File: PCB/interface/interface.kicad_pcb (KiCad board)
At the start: 2 copper layers, 100 x 100 mm, 120 parts, among them J1 24VAC, J10 RS485, J2 Brake, J3 Motor, J4 Limit, J5 LED_G, J6 Ground, J7 LED_B, J8 UART, J9 POT, K1 G2R-1-E, K2 G2R-1-E, K3 G2R-1-E, K4 G2R-1-E, SW1 SW_SPST, U1 DCDC-isolator, U10 PC817, U11 74HCT595, U12 ESP-07, U13 AT24C64, U14 LM358, U15 HCNR201, U16 PC817, U17 LM358, U18 6N137, U19 MAX485E, U2 L7812, U20 6N137, U3 DCDC-isolator, U4 ULN2003A, U5 AMS1117-3.3, U6 PC817, U7 PC817, U8 PC817, U9 PC817

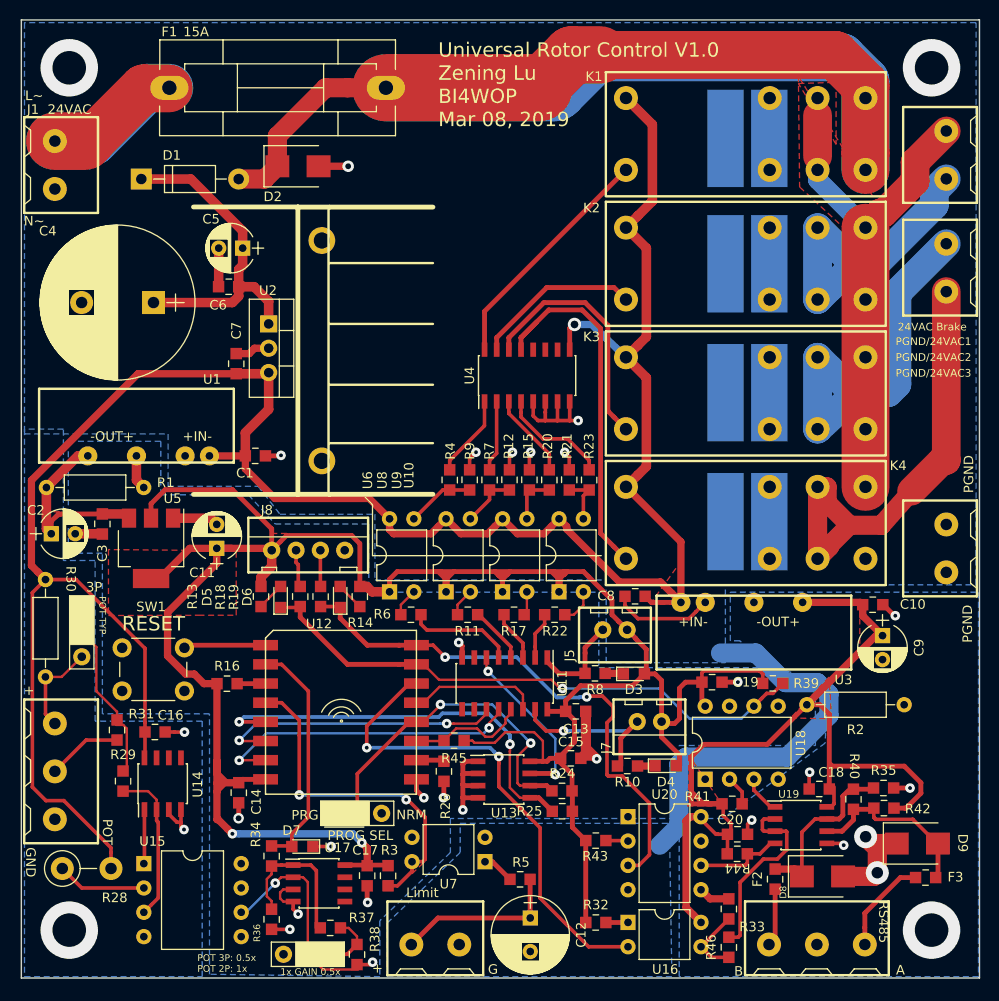
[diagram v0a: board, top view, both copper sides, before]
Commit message: New schemetic and PCB with support of Ethernet LAN connection
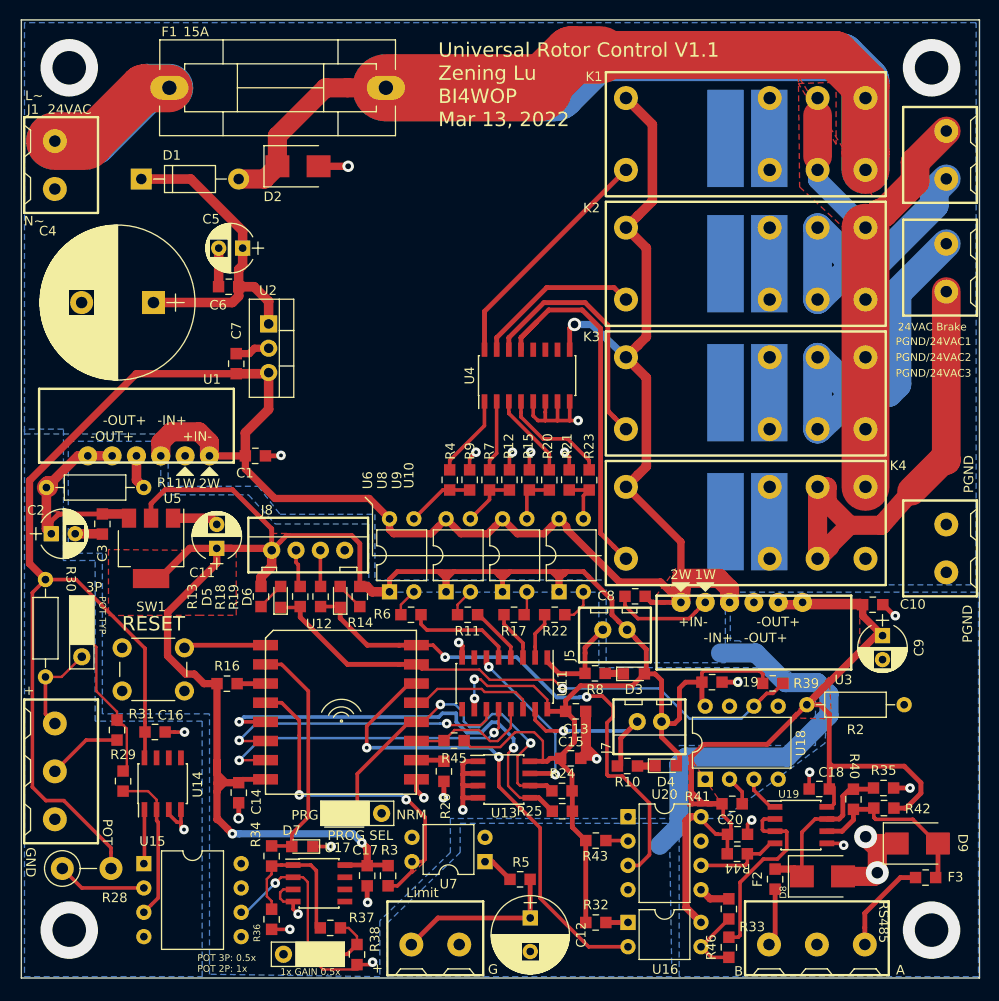
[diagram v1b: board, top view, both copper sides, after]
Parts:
- removed Ref**: Heatsink_23mm_2P, MyPCBLib:Heatsink_23mm_2P
- R1, R2: value 220 -> 10K
- R37, R38: value 8K2 -> 18K
- R41: value 470 -> 1K
- R43: value 220 -> 200
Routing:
- net +24V: track 245.6 -> 264.1 mm
- net +3V3: track 266.2 -> 279.2 mm, vias 2 -> 4
- net +5VD: track 100.9 -> 109.9 mm
- net +5V: track 20.6 -> 23.7 mm
- net /SDA: track 43.3 -> 45.2 mm
- net /SCL: track 35.6 -> 37.3 mm
- net Net-(R45-Pad2): track 12.5 -> 13.3 mm
- net Net-(U11-Pad12): track 32.6 -> 33.2 mm
- net Net-(U11-Pad11): track 30.2 -> 30.7 mm
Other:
- board text added: "Universal Rotor Control V1.1 Zening Lu BI4WOP Mar 13, 2022"
- board text removed: "Universal Rotor Control V1.0 Zening Lu BI4WOP Mar 08, 2019"
